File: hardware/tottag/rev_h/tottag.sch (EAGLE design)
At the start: 207 parts, among them J1 USB4110-GF-A, J2 DM3AT-SF-PEJM5, J3 TC2030-JLINK-NL-2SIDE, J4 TC2030-JLINK-NL-2SIDE, J5 MOLEX-PICO-SPOX-3SIDE, Q1 CSD75207W15, Q2 CSD75207W15, T1 HHM1595A1, U1 DW1000, U10 STM32F091CC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

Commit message: rev_h: add 9-DOF
quite unsure about this 'sensehub' business :/
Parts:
- removed GPIO0, GPIO1, TP7, TP8, TP9: TEST-POINT, headers:TEST-POINT
- added C93, C94, C95: 0.1uF, passives:CAPACITOR0402_CAP
- added GP0, GP1, TP28, TP29: TEST-POINT, headers:TEST-POINT
- added R38, R39: 10k, passives:RESISTOR0402_RES
- added U12: LIS3MDL, chips:LIS3MDL
- C87: value 10uF -> 1uF; device passives:CAPACITOR0603_CAP -> passives:CAPACITOR0402_CAP; DIGIKEY 1253-CM105X5R106M25ATCT-ND -> 490-7195-1-ND; MPN CM105X5R106M25AT -> GRM155R70G105KA12D
- U3: value LIS2DW12 -> LSM6DSOXTR; device chips:LIS2DW12 -> chips:LSM6DSOXTR
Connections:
- net LED_BLUE renamed STM_LED_BLUE
- net LED_GREEN renamed STM_LED_GREEN
- net LED_RED renamed STM_LED_RED
- net N$59 renamed LED_NRF_RED_COMM
- net N$60 renamed LED_NRF_GREEN_COMM
- net N$61 renamed LED_NRF_BLUE_COMM
- removed net N$23: D3.G, R12.1, TP7.TESTPOINT
- removed net N$24: D3.B, R13.1, TP9.TESTPOINT
- removed net N$25: D3.R, R11.1, TP8.TESTPOINT
- new net LSM_SENSEHUB_SCL: R39.2, TP28.TESTPOINT, U12.SCL/SPC, U3.SCX
- new net LSM_SENSEHUB_SDA: R38.2, TP29.TESTPOINT, U12.SDA/SDI/SDO, U3.SDX
- new net MAG_DRDY: U12.DRDY, U7.P1.00
- new net MAG_INT: U12.INT, U7.P0.23
- new net N$33: C94.1, U12.C1
- new net STM_LED_BLUE_COMM: D3.B, R13.1
- new net STM_LED_GREEN_COMM: D3.G, R12.1
- new net STM_LED_RED_COMM: D3.R, R11.1
- net !NRF_CS_SD: now also U7.P0.13; no longer U7.P0.20
- net +3V3: now also C38.2, C93.1, C95.1, R38.1, R39.1, U12.CS, U12.VDD, U12.VDD_IO, U3.VDD, U3.VDDIO; no longer C38.1, U3.VCC, U3.VDD_IO
- net GND: now also C38.1, C93.2, C94.2, C95.2, U12.GND, U12.SDO/SA1, U3.GND_2; no longer C38.2
- net GPIO0: now also GP0.TESTPOINT; no longer GPIO0.TESTPOINT
- net GPIO1: now also GP1.TESTPOINT; no longer GPIO1.TESTPOINT
- net NRF_IMU_INT1: now also U7.P0.17; no longer U7.P0.22
- net NRF_IMU_INT2: now also U7.P0.15; no longer U7.P0.24
- net NRF_SPI0_MISO: now also U3.SDO/SA0, U7.P0.24; no longer U3.MISO/SA0, U7.P0.15
- net NRF_SPI0_MOSI: now also U3.SDA, U7.P0.22; no longer U3.MOSI/SDA, U7.P0.13
- net NRF_SPI0_SCLK: now also U3.SCL, U7.P0.20; no longer U3.SCL/SPC, U7.P0.17
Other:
- note added: "Accelerometer + Gyro"
- note added: "Magnetometer"
- note removed: "Accelerometer"

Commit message: rev_h: renumber passives
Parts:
- C66, C67: value 470nF -> 0.1uF; DIGIKEY 490-12270-1-ND -> 490-6328-1-ND; MPN GRT155R61E474ME01D -> GRM155R71C104KA88J
- C68: value 1uF -> 0.1uF; DIGIKEY (none) -> 490-6328-1-ND; MPN (none) -> GRM155R71C104KA88J
- C69: value 1uF -> 470nF; DIGIKEY 490-7195-1-ND -> 490-12270-1-ND; MPN GRM155R70G105KA12D -> GRT155R61E474ME01D
- C70: value 1uF -> 470nF; DIGIKEY (none) -> 490-12270-1-ND; MPN (none) -> GRT155R61E474ME01D
- C71, C73, C75: DIGIKEY 490-7195-1-ND -> (none); MPN GRM155R70G105KA12D -> (none)
- C72: DIGIKEY (none) -> 490-7195-1-ND; MPN (none) -> GRM155R70G105KA12D
- C76, C77, C79: value 4.7uF -> 1uF; DIGIKEY (none) -> 490-7195-1-ND; MPN (none) -> GRM155R70G105KA12D
- C78: value 4.7uF -> 1uF; DESCRIPTION CAP CER 4.7UF 6.3V X5R 0402 -> (none); DIGIKEY 445-5947-1-ND -> 490-7195-1-ND; MANUFACTURER TDK -> (none); MPN C1005X5R0J475K050BC -> GRM155R70G105KA12D
- C82: DESCRIPTION (none) -> CAP CER 4.7UF 6.3V X5R 0402; DIGIKEY (none) -> 445-5947-1-ND; MANUFACTURER (none) -> TDK; MPN (none) -> C1005X5R0J475K050BC
- C85, C86: DESCRIPTION CAP CER 4.7UF 6.3V X5R 0402 -> (none); DIGIKEY 445-5947-1-ND -> (none); MANUFACTURER TDK -> (none); MPN C1005X5R0J475K050BC -> (none)
- C87: value 1uF -> 4.7uF; DIGIKEY 490-7195-1-ND -> (none); MPN GRM155R70G105KA12D -> (none)
- C88: value 10uF -> 4.7uF; device passives:CAPACITOR0603_CAP -> passives:CAPACITOR0402_CAP; DIGIKEY 1253-CM105X5R106M25ATCT-ND -> (none); MPN CM105X5R106M25AT -> (none)
- C89, C90: value 10uF -> 4.7uF; device passives:CAPACITOR0603_CAP -> passives:CAPACITOR0402_CAP; DESCRIPTION (none) -> CAP CER 4.7UF 6.3V X5R 0402; DIGIKEY 1253-CM105X5R106M25ATCT-ND -> 445-5947-1-ND; MANUFACTURER (none) -> TDK; MPN CM105X5R106M25AT -> C1005X5R0J475K050BC
- C92: value 47uF -> 10uF; DIGIKEY 490-13247-1-ND -> 1253-CM105X5R106M25ATCT-ND; MPN GRM188R60J476ME15D -> CM105X5R106M25AT
- C93, C94: value 0.1uF -> 10uF; device passives:CAPACITOR0402_CAP -> passives:CAPACITOR0603_CAP; DIGIKEY 490-6328-1-ND -> 1253-CM105X5R106M25ATCT-ND; MPN GRM155R71C104KA88J -> CM105X5R106M25AT
- C95: value 0.1uF -> 47uF; device passives:CAPACITOR0402_CAP -> passives:CAPACITOR0603_CAP; DIGIKEY 490-6328-1-ND -> 490-13247-1-ND; MPN GRM155R71C104KA88J -> GRM188R60J476ME15D
- R25, R26: value 11k -> 10k; DIGIKEY RMCF0402FT11K0CT-ND -> 311-10KJRCT-ND; MPN RMCF0402FT11K0 -> RC0402JR-0710KL
- R27: value 16k -> 11k; DIGIKEY RMCF0402FT16K0CT-ND -> RMCF0402FT11K0CT-ND; MPN RMCF0402FT16K0 -> RMCF0402FT11K0
- R28: value 100k -> 11k; DIGIKEY (none) -> RMCF0402FT11K0CT-ND; MPN (none) -> RMCF0402FT11K0
- R29: value 100k -> 16k; DIGIKEY (none) -> RMCF0402FT16K0CT-ND; MPN (none) -> RMCF0402FT16K0
- R35: value 3.3M -> 100k; DIGIKEY RMCF0402FT3M30CT-ND -> (none); MPN RMCF0402FT3M30 -> (none)
- R36: value 10M -> 100k; DIGIKEY RMCF0402FT10M0CT-ND -> (none); MPN RMCF0402FT10M0 -> (none)
- R37: value DNP -> 3.3M; DIGIKEY (none) -> RMCF0402FT3M30CT-ND; MPN (none) -> RMCF0402FT3M30
- R38: value 10k -> 10M; DIGIKEY 311-10KJRCT-ND -> RMCF0402FT10M0CT-ND; MPN RC0402JR-0710KL -> RMCF0402FT10M0
- R39: value 10k -> DNP; DIGIKEY 311-10KJRCT-ND -> (none); MPN RC0402JR-0710KL -> (none)
- R7: DIGIKEY RMCF0402FT1K00CT-ND -> (none); MPN RMCF0402FT1K00 -> (none)
- R8: DIGIKEY (none) -> RMCF0402FT1K00CT-ND; MPN (none) -> RMCF0402FT1K00
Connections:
- net !NRF_CS_RTC: now also R36.2; no longer R34.2
- net !NRF_CS_SD: now also R33.1; no longer R31.1
- net !SD_DETECT: now also R31.1; no longer R29.1
- net +1V8: now also C84.1, C91.1; no longer C80.1, C88.1
- net +3V3: now also C66.1, C74.1, C76.1, C85.1, C86.1, C88.1, R25.1, R26.1, R36.1, R7.1; no longer C70.1, C77.1, C82.1, C84.1, C92.1, C93.1, R10.1, R34.1, R38.1, R39.1
- net BATIN: now also R37.1, R38.2; no longer R35.1, R36.2
- net BQ_AC1: now also C69.2; no longer C66.2
- net BQ_AC2: now also C70.2; no longer C67.2
- net BQ_CLAMP1: now also C69.1; no longer C66.1
- net BQ_CLAMP2: now also C70.1; no longer C67.1
- net BQ_RECT: now also C92.1, C93.1; no longer C89.1, C90.1
- net DW_IRQ: now also R35.2; no longer R33.2
- net GND: now also C66.2, C67.2, C72.2, C75.1, R27.1, R30.2, R35.1, R38.1, R39.1; no longer C69.2, C70.2, C72.1, C75.2, R25.1, R26.2, R33.1, R36.1, R37.1
- net LED_NRF_BLUE: now also R10.2; no longer R9.2
- net LED_NRF_BLUE_COMM: now also R10.1; no longer R9.1
- net LED_NRF_GREEN: now also R9.2; no longer R8.2
- net LED_NRF_GREEN_COMM: now also R9.1; no longer R8.1
- net LED_NRF_RED: now also R8.2; no longer R7.2
- net LED_NRF_RED_COMM: now also R8.1; no longer R7.1
- net LSM_SENSEHUB_SCL: now also R26.2; no longer R39.2
- net LSM_SENSEHUB_SDA: now also R25.2; no longer R38.2
- net N$12: now also R29.2; no longer R27.2
- net N$16: now also R29.1; no longer R27.1
- net N$21: now also R27.2; no longer R25.2
- net N$22: now also R28.1; no longer R26.1
- net N$33: now also C67.1; no longer C94.1
- net N$49: now also R39.2; no longer R37.2
- net N$54: now also R7.2; no longer R10.2
- net NRF_DECAP46: now also C72.1; no longer C69.1
- net NRF_DECUSB: now also C89.1; no longer C85.1
- net NRF_SPI2_MISO: now also R34.1; no longer R32.1
- net NRF_SPI2_MOSI: now also R32.1; no longer R30.1
- net SD_EN: now also R30.1; no longer R28.1
- net VBAT: now also C78.1, R37.2; no longer C75.1, R35.2
- net VBAT_SWITCHED: now also C80.1; no longer C76.1
- net VCC_SDCARD: now also C82.1, R33.2, R34.2; no longer C78.1, R29.2, R30.2
- net VQI: now also C77.1, C94.1; no longer C74.1, C91.1
- net VUSB: now also C75.2; no longer C72.2
- net VUSB_NRF: now also C90.1; no longer C86.1
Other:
- moved on the sheet: C71, C75, C77, C84, C88, R27, R30, R31, R32, R37, R8, R9

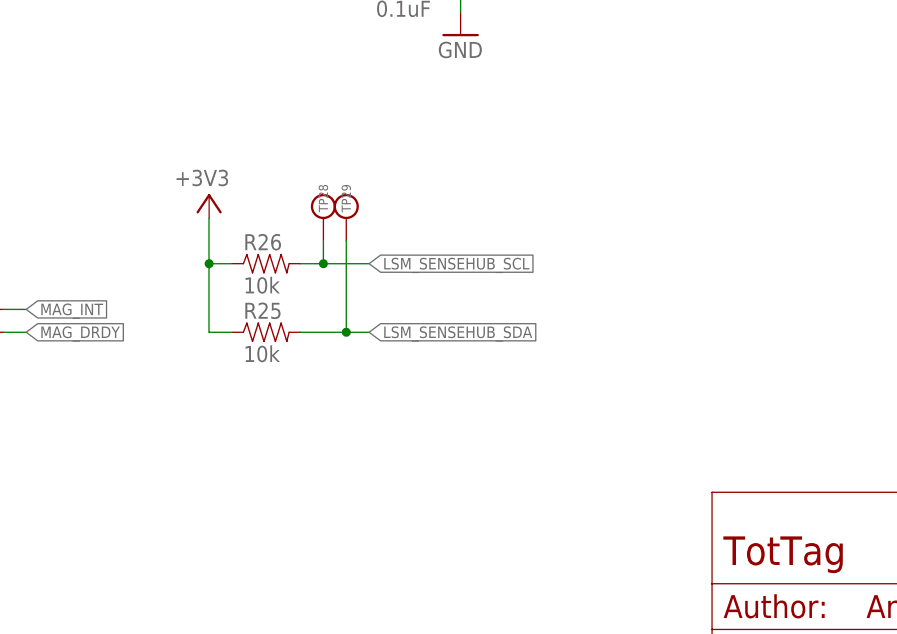
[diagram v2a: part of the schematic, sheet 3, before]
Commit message: rev_h: wire mag DRDY to 6dof MRDRY pin
*now* this connection makes sense to me
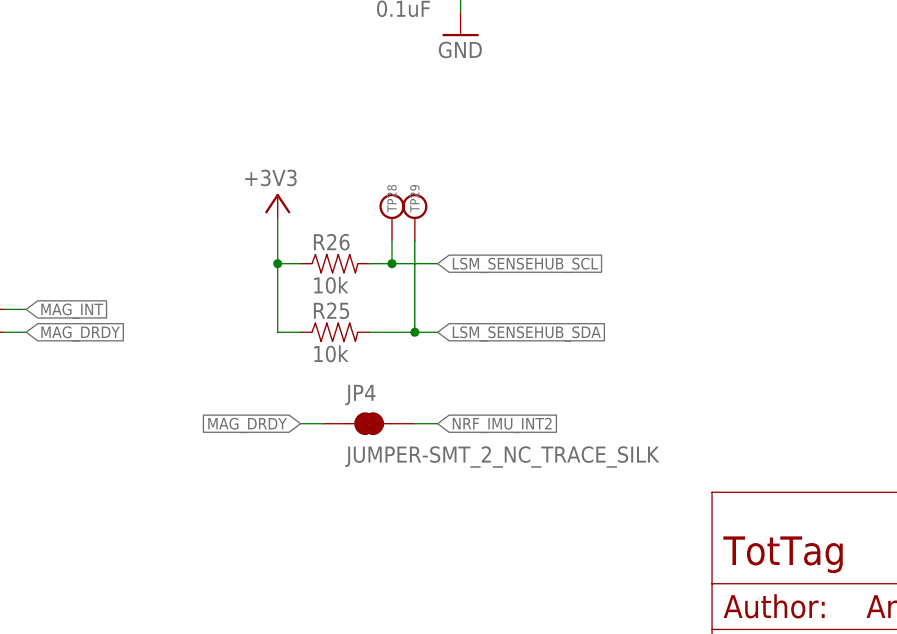
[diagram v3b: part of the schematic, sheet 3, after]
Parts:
- added JP4: JUMPER-SMT_2_NC_TRACE_SILK, SparkFun-Jumpers:JUMPER-SMT_2_NC_TRACE_SILK
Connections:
- net MAG_DRDY: now also JP4.1
- net NRF_IMU_INT2: now also JP4.2
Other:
- note added: "In Mode 2, INT2 pin is also the "I2C master exteranal sync signal" aka MDRDY. But make this easy to cut, just in case."
- moved on the sheet: R25, R26, TP28, TP29
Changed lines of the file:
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@@
 <part name="TP29" library="headers" deviceset="TEST-POINT" device=""/>
 <part name="P+15" library="regulators" deviceset="+3V3" device=""/>
+<part name="JP4" library="SparkFun-Jumpers" library_urn="urn:adsk.eagle:library:528" deviceset="JUMPER-SMT_2_NC_TRACE" device="_SILK" package3d_urn="urn:adsk.eagle:package:39281/1"/>
 </parts>
 <sheets>
@@
 <wire x1="251.46" y1="134.62" x2="0" y2="134.62" width="0.254" layer="98" style="shortdash"/>
 <text x="44.196" y="52.324" size="3.81" layer="98">Magnetometer</text>
+<text x="116.84" y="22.606" size="1.27" layer="98" align="top-center">In Mode 2, INT2 pin is also the
+"I2C master exteranal sync signal"
+aka MDRDY. But make this easy to
+cut, just in case.</text>
 </plain>
 <instances>
@@
 <attribute name="VALUE" x="48.26" y="20.32" size="1.778" layer="95"/>
 </instance>
-<instance part="R25" gate="G$1" x="106.68" y="38.1" smashed="yes">
-<attribute name="DIGIKEY" x="106.68" y="38.1" size="1.778" layer="96" display="off"/>
-<attribute name="MPN" x="106.68" y="38.1" size="1.778" layer="96" display="off"/>
-<attribute name="NAME" x="102.87" y="39.5986" size="1.778" layer="95"/>
-<attribute name="VALUE" x="102.87" y="34.798" size="1.778" layer="96"/>
-</instance>
-<instance part="R26" gate="G$1" x="106.68" y="45.72" smashed="yes">
-<attribute name="DIGIKEY" x="106.68" y="45.72" size="1.778" layer="96" display="off"/>
-<attribute name="MPN" x="106.68" y="45.72" size="1.778" layer="96" display="off"/>
-<attribute name="NAME" x="102.87" y="47.2186" size="1.778" layer="95"/>
-<attribute name="VALUE" x="102.87" y="42.418" size="1.778" layer="96"/>
+<instance part="R25" gate="G$1" x="114.3" y="38.1" smashed="yes">
+<attribute name="DIGIKEY" x="114.3" y="38.1" size="1.778" layer="96" display="off"/>
+<attribute name="MPN" x="114.3" y="38.1" size="1.778" layer="96" display="off"/>
+<attribute name="NAME" x="110.49" y="39.5986" size="1.778" layer="95"/>
+<attribute name="VALUE" x="110.49" y="34.798" size="1.778" layer="96"/>
+</instance>
+<instance part="R26" gate="G$1" x="114.3" y="45.72" smashed="yes">
+<attribute name="DIGIKEY" x="114.3" y="45.72" size="1.778" layer="96" display="off"/>
+<attribute name="MPN" x="114.3" y="45.72" size="1.778" layer="96" display="off"/>
+<attribute name="NAME" x="110.49" y="47.2186" size="1.778" layer="95"/>
+<attribute name="VALUE" x="110.49" y="42.418" size="1.778" layer="96"/>
 </instance>
 <instance part="C79" gate="G$1" x="27.94" y="50.8" smashed="yes" rot="R270">
@@
 <attribute name="VALUE" x="40.64" y="12.7" size="1.778" layer="96"/>
 </instance>
-<instance part="TP28" gate="G$1" x="111.76" y="50.8" smashed="yes" rot="R270">
-<attribute name="NAME" x="111.76" y="51.435" size="1.016" layer="95" ratio="12" rot="R270" align="center-right"/>
+<instance part="TP28" gate="G$1" x="119.38" y="50.8" smashed="yes" rot="R270">
+<attribute name="NAME" x="119.38" y="51.435" size="1.016" layer="95" ratio="12" rot="R270" align="center-right"/>
 </instance>
-<instance part="TP29" gate="G$1" x="114.3" y="50.8" smashed="yes" rot="R270">
-<attribute name="NAME" x="114.3" y="51.435" size="1.016" layer="95" ratio="12" rot="R270" align="center-right"/>
+<instance part="TP29" gate="G$1" x="121.92" y="50.8" smashed="yes" rot="R270">
+<attribute name="NAME" x="121.92" y="51.435" size="1.016" layer="95" ratio="12" rot="R270" align="center-right"/>
 </instance>
-<instance part="P+15" gate="P1" x="99.06" y="53.34" smashed="yes">
-<attribute name="VALUE" x="101.346" y="56.134" size="1.778" layer="96" rot="R180"/>
+<instance part="P+15" gate="P1" x="106.68" y="53.34" smashed="yes">
+<attribute name="VALUE" x="108.966" y="56.134" size="1.778" layer="96" rot="R180"/>
+</instance>
+<instance part="JP4" gate="G$1" x="116.84" y="27.94" smashed="yes">
+<attribute name="NAME" x="114.3" y="30.48" size="1.778" layer="95" font="vector"/>
+<attribute name="VALUE" x="114.3" y="25.4" size="1.778" layer="96" font="vector" align="top-left"/>
 </instance>
 </instances>
@@
 <pinref part="R26" gate="G$1" pin="1"/>
 <pinref part="P+15" gate="P1" pin="+3V3"/>
-<wire x1="101.6" y1="45.72" x2="99.06" y2="45.72" width="0.1524" layer="91"/>
-<wire x1="99.06" y1="45.72" x2="99.06" y2="50.8" width="0.1524" layer="91"/>
+<wire x1="109.22" y1="45.72" x2="106.68" y2="45.72" width="0.1524" layer="91"/>
+<wire x1="106.68" y1="45.72" x2="106.68" y2="50.8" width="0.1524" layer="91"/>
 <pinref part="R25" gate="G$1" pin="1"/>
-<wire x1="101.6" y1="38.1" x2="99.06" y2="38.1" width="0.1524" layer="91"/>
-<wire x1="99.06" y1="38.1" x2="99.06" y2="45.72" width="0.1524" layer="91"/>
-<junction x="99.06" y="45.72"/>
+<wire x1="109.22" y1="38.1" x2="106.68" y2="38.1" width="0.1524" layer="91"/>
+<wire x1="106.68" y1="38.1" x2="106.68" y2="45.72" width="0.1524" layer="91"/>
+<junction x="106.68" y="45.72"/>
 </segment>
 </net>
@@
 <pinref part="U3" gate="A" pin="INT2"/>
 </segment>
+<segment>
+<wire x1="121.92" y1="27.94" x2="124.46" y2="27.94" width="0.1524" layer="91"/>
+<label x="124.46" y="27.94" size="1.27" layer="95" xref="yes"/>
+<pinref part="JP4" gate="G$1" pin="2"/>
+</segment>
 </net>
 <net name="NRF_SPI0_MISO" class="0">
@@
 <segment>
 <pinref part="R25" gate="G$1" pin="2"/>
-<wire x1="109.22" y1="38.1" x2="114.3" y2="38.1" width="0.1524" layer="91"/>
-<label x="116.84" y="38.1" size="1.27" layer="95" xref="yes"/>
+<wire x1="116.84" y1="38.1" x2="121.92" y2="38.1" width="0.1524" layer="91"/>
+<label x="124.46" y="38.1" size="1.27" layer="95" xref="yes"/>
 <pinref part="TP29" gate="G$1" pin="TESTPOINT"/>
-<wire x1="114.3" y1="38.1" x2="116.84" y2="38.1" width="0.1524" layer="91"/>
-<wire x1="114.3" y1="38.1" x2="114.3" y2="48.26" width="0.1524" layer="91"/>
-<junction x="114.3" y="38.1"/>
+<wire x1="121.92" y1="38.1" x2="124.46" y2="38.1" width="0.1524" layer="91"/>
+<wire x1="121.92" y1="38.1" x2="121.92" y2="48.26" width="0.1524" layer="91"/>
+<junction x="121.92" y="38.1"/>
 </segment>
 </net>
@@
 <segment>
 <pinref part="R26" gate="G$1" pin="2"/>
-<wire x1="109.22" y1="45.72" x2="111.76" y2="45.72" width="0.1524" layer="91"/>
-<label x="116.84" y="45.72" size="1.27" layer="95" xref="yes"/>
+<wire x1="116.84" y1="45.72" x2="119.38" y2="45.72" width="0.1524" layer="91"/>
+<label x="124.46" y="45.72" size="1.27" layer="95" xref="yes"/>
 <pinref part="TP28" gate="G$1" pin="TESTPOINT"/>
-<wire x1="111.76" y1="45.72" x2="116.84" y2="45.72" width="0.1524" layer="91"/>
-<wire x1="111.76" y1="45.72" x2="111.76" y2="48.26" width="0.1524" layer="91"/>
-<junction x="111.76" y="45.72"/>
+<wire x1="119.38" y1="45.72" x2="124.46" y2="45.72" width="0.1524" layer="91"/>
+<wire x1="119.38" y1="45.72" x2="119.38" y2="48.26" width="0.1524" layer="91"/>
+<junction x="119.38" y="45.72"/>
 </segment>
 </net>
@@
 <label x="78.74" y="38.1" size="1.27" layer="95" xref="yes"/>
 </segment>
+<segment>
+<wire x1="111.76" y1="27.94" x2="109.22" y2="27.94" width="0.1524" layer="91"/>
+<label x="109.22" y="27.94" size="1.27" layer="95" rot="R180" xref="yes"/>
+<pinref part="JP4" gate="G$1" pin="1"/>
+</segment>
 </net>

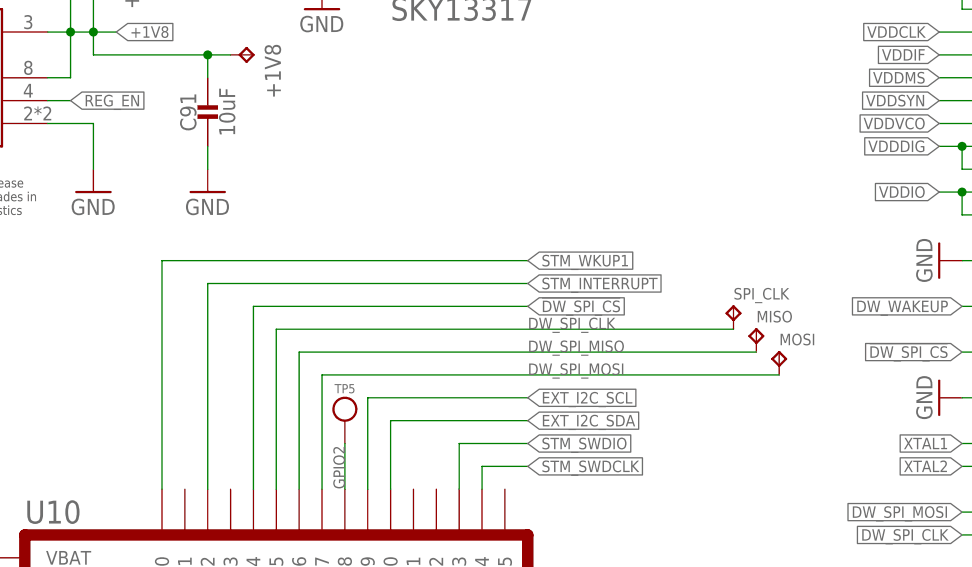
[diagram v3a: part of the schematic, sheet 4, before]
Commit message: rev_h: add last missing test point
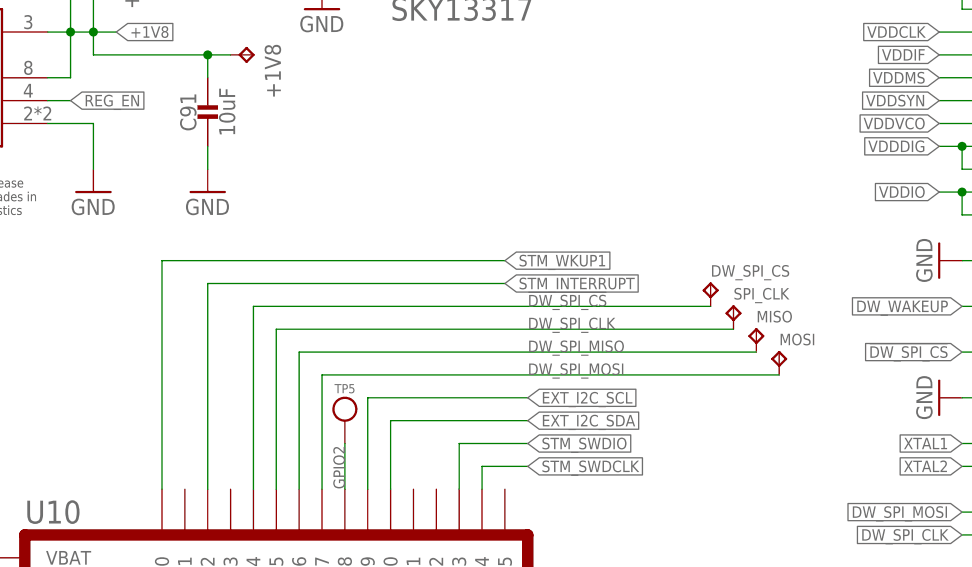
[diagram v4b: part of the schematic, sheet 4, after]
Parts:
- added DW_SPI_CS: TPTP06SQ, testpad:TPTP06SQ
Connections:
- net !DW_SPI_CS: now also DW_SPI_CS.TP
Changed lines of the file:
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@@
 <part name="P+15" library="regulators" deviceset="+3V3" device=""/>
 <part name="JP4" library="SparkFun-Jumpers" library_urn="urn:adsk.eagle:library:528" deviceset="JUMPER-SMT_2_NC_TRACE" device="_SILK" package3d_urn="urn:adsk.eagle:package:39281/1"/>
+<part name="DW_SPI_CS" library="testpad" library_urn="urn:adsk.eagle:library:385" deviceset="TP" device="TP06SQ" package3d_urn="urn:adsk.eagle:package:27952/1"/>
 </parts>
 <sheets>
@@
 <attribute name="MPN" x="76.2" y="149.86" size="1.27" layer="96" align="top-left" display="off"/>
 </instance>
+<instance part="DW_SPI_CS" gate="G$1" x="132.08" y="129.54" smashed="yes">
+<attribute name="NAME" x="132.08" y="130.302" size="1.27" layer="95"/>
+<attribute name="TP_SIGNAL_NAME" x="133.35" y="128.27" size="1.778" layer="97"/>
+</instance>
 </instances>
 <busses>
@@
 <net name="STM_INTERRUPT" class="0">
 <segment>
-<wire x1="76.2" y1="129.54" x2="111.76" y2="129.54" width="0.1524" layer="91"/>
-<label x="111.76" y="129.54" size="1.27" layer="95" xref="yes"/>
+<wire x1="76.2" y1="129.54" x2="109.22" y2="129.54" width="0.1524" layer="91"/>
+<label x="109.22" y="129.54" size="1.27" layer="95" xref="yes"/>
 <pinref part="U10" gate="U1" pin="PA2"/>
 <wire x1="76.2" y1="106.68" x2="76.2" y2="129.54" width="0.1524" layer="91"/>
@@
 <pinref part="U10" gate="U1" pin="PA4"/>
 <wire x1="81.28" y1="106.68" x2="81.28" y2="127" width="0.1524" layer="91"/>
-<wire x1="81.28" y1="127" x2="111.76" y2="127" width="0.1524" layer="91"/>
-<label x="111.76" y="127" size="1.27" layer="95" xref="yes"/>
+<wire x1="81.28" y1="127" x2="132.08" y2="127" width="0.1524" layer="91"/>
+<label x="111.76" y="127" size="1.27" layer="95"/>
+<pinref part="DW_SPI_CS" gate="G$1" pin="TP"/>
 </segment>
 <segment>
@@
 <pinref part="U10" gate="U1" pin="PA0"/>
 <wire x1="71.12" y1="106.68" x2="71.12" y2="132.08" width="0.1524" layer="91"/>
-<wire x1="71.12" y1="132.08" x2="111.76" y2="132.08" width="0.1524" layer="91"/>
-<label x="111.76" y="132.08" size="1.27" layer="95" xref="yes"/>
+<wire x1="71.12" y1="132.08" x2="109.22" y2="132.08" width="0.1524" layer="91"/>
+<label x="109.22" y="132.08" size="1.27" layer="95" xref="yes"/>
 </segment>
 </net>
